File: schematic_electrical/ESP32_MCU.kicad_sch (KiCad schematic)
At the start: 4 parts, among them U1 ESP32_S3_LOLIN

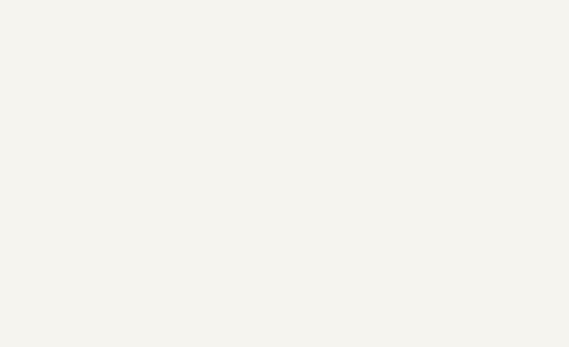
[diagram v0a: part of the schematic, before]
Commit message: Pylon schmatic: clarify filenames and add orange text to avoid confusing other similar schematic pages.
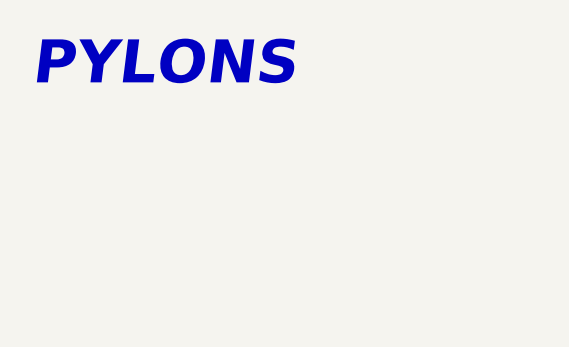
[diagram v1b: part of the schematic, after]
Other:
- note added: "PYLONS"
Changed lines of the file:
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@@
+		)
+	)
+	(text "PYLONS"
+		(exclude_from_sim no)
+		(at 29.972 23.368 0)
+		(effects
+			(font
+				(size 4.7752 4.7752)
+				(thickness 0.955)
+				(bold yes)
+				(italic yes)
+				(color 255 153 0 1)
+			)
 		)
 	)
@@
 		)
 		(instances
-			(project "high_striker_boosh"
+			(project "pylons_boosh_remote_reciver"
 				(path "/f3653ac0-a28a-4ee8-bcf5-236139001455/91617d0d-6f07-4f47-baaa-678bb3c8f5f7"
 					(reference "#PWR02")
@@
 		)
 		(instances
-			(project "high_striker_boosh"
+			(project "pylons_boosh_remote_reciver"
 				(path "/f3653ac0-a28a-4ee8-bcf5-236139001455/91617d0d-6f07-4f47-baaa-678bb3c8f5f7"
 					(reference "#PWR01")
@@
 		)
 		(instances
-			(project "high_striker_boosh"
+			(project "pylons_boosh_remote_reciver"
 				(path "/f3653ac0-a28a-4ee8-bcf5-236139001455/91617d0d-6f07-4f47-baaa-678bb3c8f5f7"
 					(reference "U1")
@@
 		)
 		(instances
-			(project "high_striker_boosh"
+			(project "pylons_boosh_remote_reciver"
 				(path "/f3653ac0-a28a-4ee8-bcf5-236139001455/91617d0d-6f07-4f47-baaa-678bb3c8f5f7"
 					(reference "R11")
@@
 		)
 		(instances
-			(project "high_striker_boosh"
+			(project "pylons_boosh_remote_reciver"
 				(path "/f3653ac0-a28a-4ee8-bcf5-236139001455/91617d0d-6f07-4f47-baaa-678bb3c8f5f7"
 					(reference "#PWR07")
@@
 		)
 		(instances
-			(project "high_striker_boosh"
+			(project "pylons_boosh_remote_reciver"
 				(path "/f3653ac0-a28a-4ee8-bcf5-236139001455/91617d0d-6f07-4f47-baaa-678bb3c8f5f7"
 					(reference "R12")
@@
 		)
 		(instances
-			(project "high_striker_boosh"
+			(project "pylons_boosh_remote_reciver"
 				(path "/f3653ac0-a28a-4ee8-bcf5-236139001455/91617d0d-6f07-4f47-baaa-678bb3c8f5f7"
 					(reference "#PWR04")
@@
 		)
 		(instances
-			(project "high_striker_boosh"
+			(project "pylons_boosh_remote_reciver"
 				(path "/f3653ac0-a28a-4ee8-bcf5-236139001455/91617d0d-6f07-4f47-baaa-678bb3c8f5f7"
 					(reference "R13")
@@
 		)
 		(instances
-			(project "high_striker_boosh"
+			(project "pylons_boosh_remote_reciver"
 				(path "/f3653ac0-a28a-4ee8-bcf5-236139001455/91617d0d-6f07-4f47-baaa-678bb3c8f5f7"
 					(reference "#PWR03")

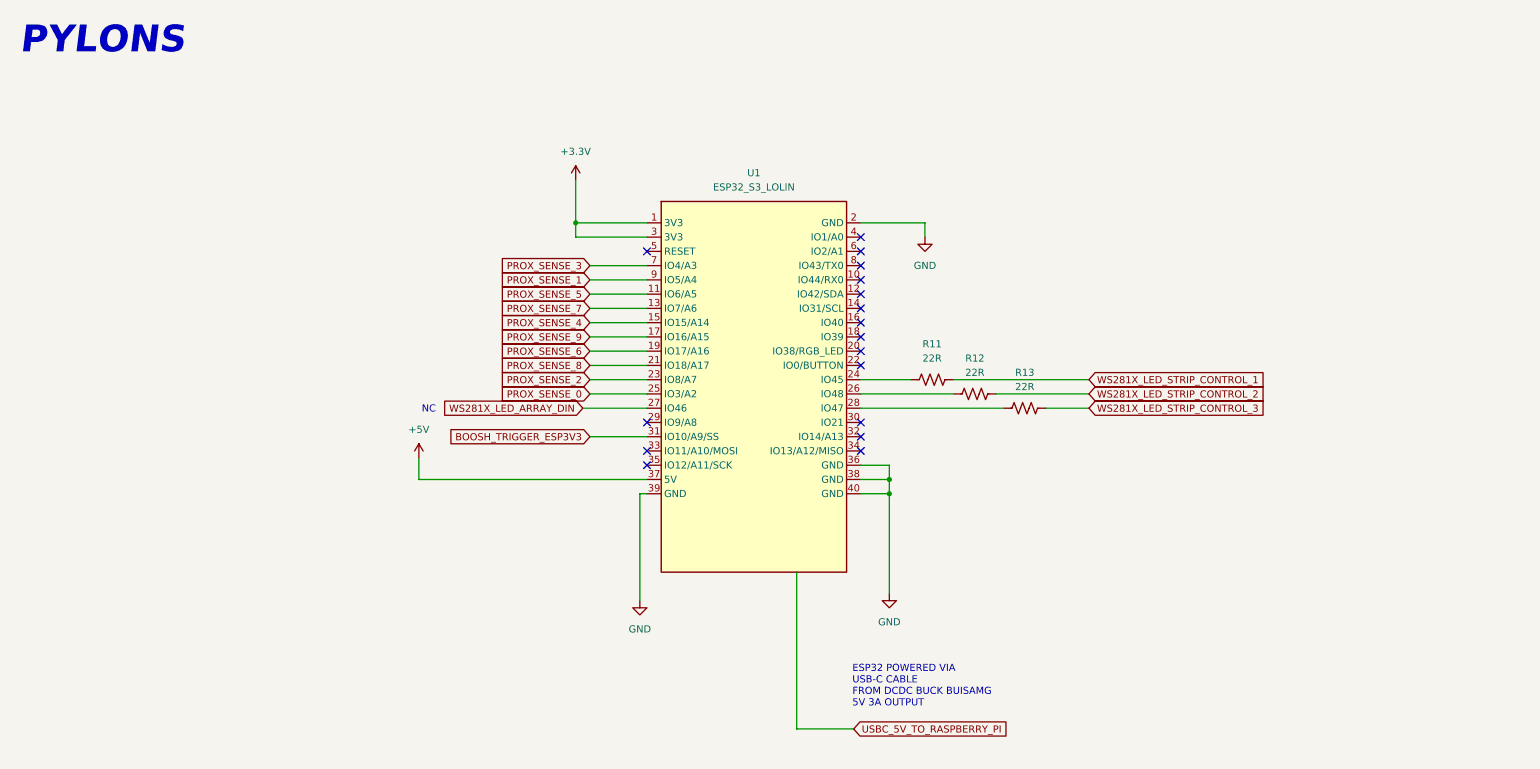
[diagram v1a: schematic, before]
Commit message: Schematic for fabrication. New symbols
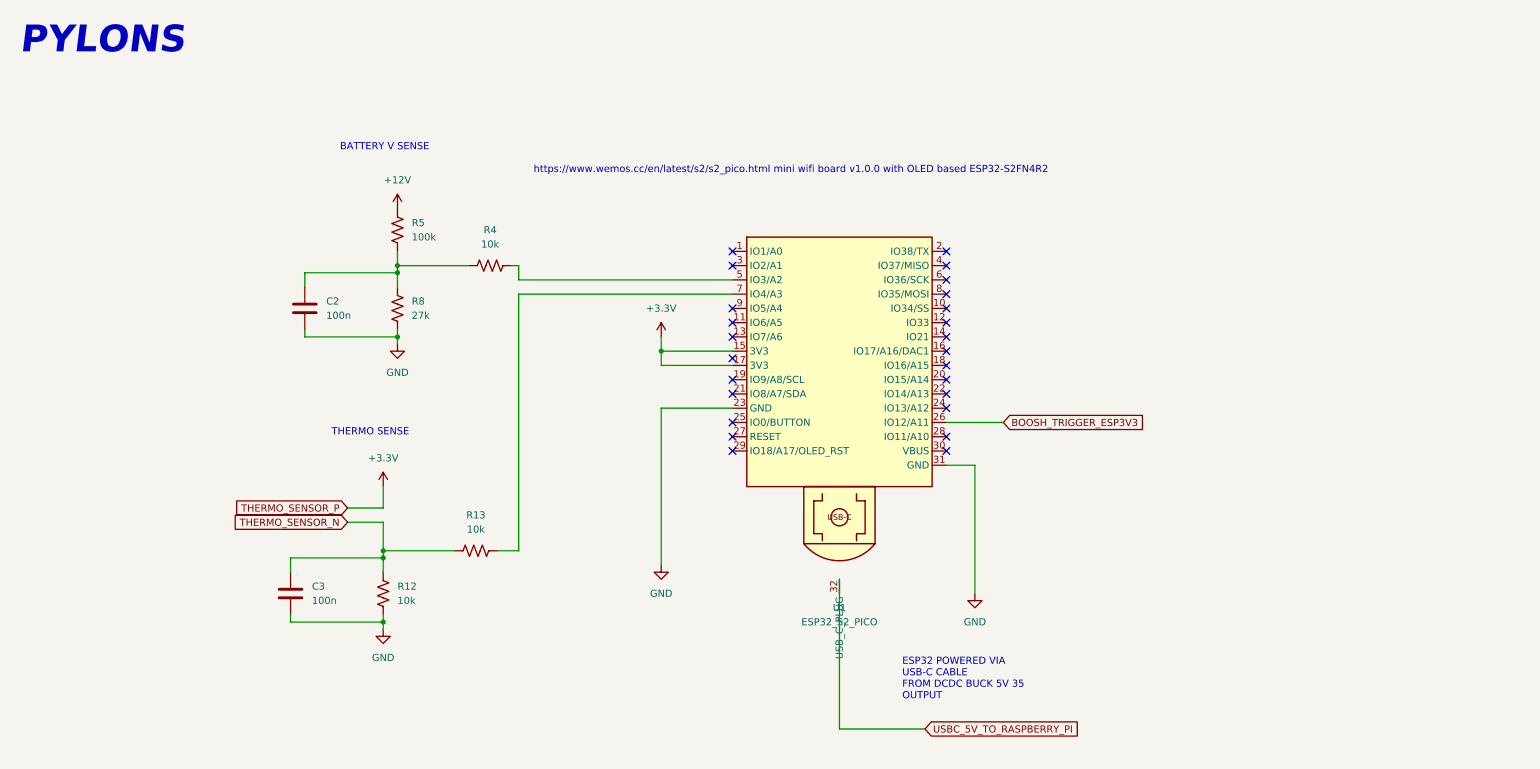
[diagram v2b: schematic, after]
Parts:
- removed R11: 22R, symbol Device:R_US
- removed U1: ESP32_S3_LOLIN, Module:ESP32 S3 LOLIN, symbol esp32 s3 lolin:ESP32_S3_LOLIN
- added C2, C3: 100n, symbol Device:C
- added R4: 10k, symbol Device:R_US
- added R5: 100k, symbol Device:R_US
- added R8: 27k, symbol Device:R_US
- added U1: ESP32_S2_PICO, Module:ESP32_S2_PICO, symbol esp32_s2_pico:ESP32_S2_PICO
- R12, R13: value 22R -> 10k
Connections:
- net WS281X_LED_STRIP_CONTROL_2 is gone; now on net GND: R12.2
- net +3.3V: now also U1.15 (3V3), U1.17 (3V3)
- net BOOSH_TRIGGER_ESP3V3: now also U1.26 (IO12/A11)
- net GND: now also C2.2, C3.2, R8.2, U1.23 (GND), U1.31 (GND)
- net USBC_5V_TO_RASPBERRY_PI: now also U1.32 (USB_C_PLUG)
- net THERMO_SENSOR_N: now reaches R12.1
- net THERMO_SENSOR_N: now also R13.1, C3.1
- net WS281X_LED_STRIP_CONTROL_3: no longer names the net of R13.2
- net WS281X_LED_STRIP_CONTROL_3: now also U1.7 (IO4/A3)
- new net: C2.1, R4.1, R5.2, R8.1
- new net: R4.2, U1.5 (IO3/A2)
- new net +12V: R5.1
- no-connect marks 17 -> 25
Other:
- note added: "BATTERY V SENSE"
- note added: "THERMO SENSE"
- note added: "https://www.wemos.cc/en/latest/s2/s2_pico.html mini wifi board v1.0.0 with OLED based ESP32-S2FN4R2"
- note removed: "NC"

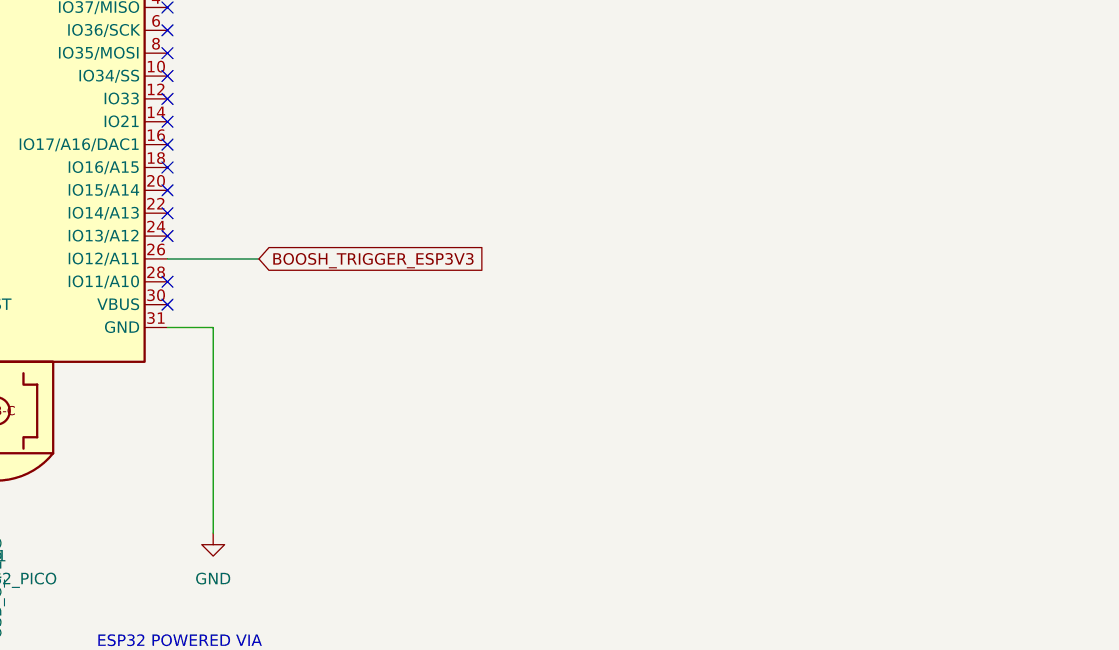
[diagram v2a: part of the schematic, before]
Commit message: scehmatic power options cleanup and LED actual as built
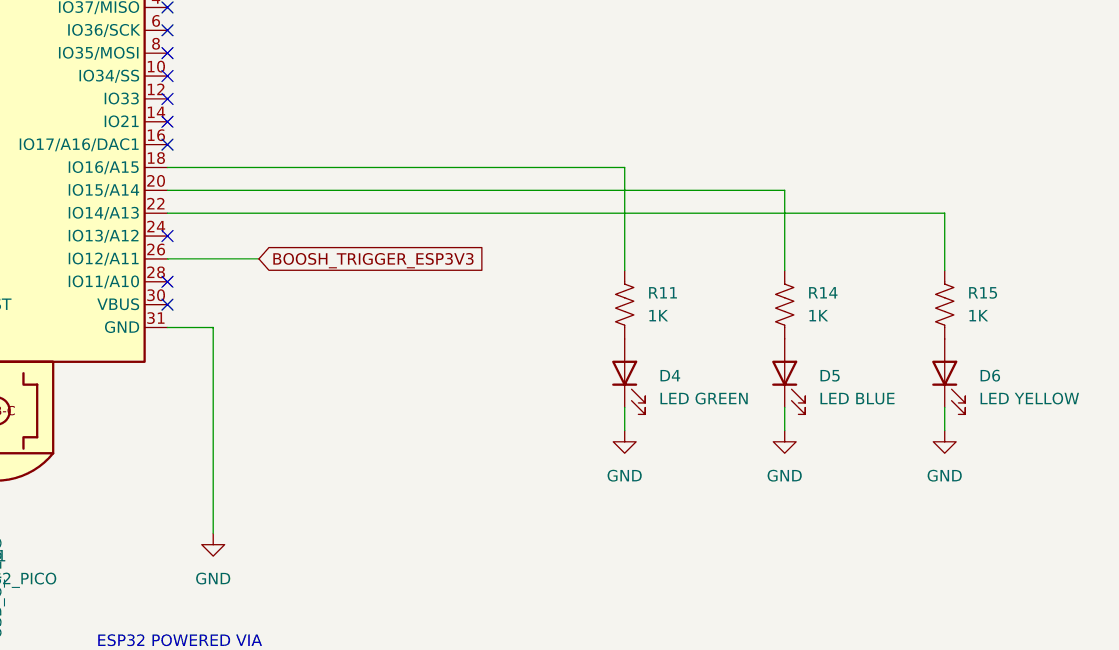
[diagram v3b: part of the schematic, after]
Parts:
- added D4: LED GREEN, symbol Device:LED
- added D5: LED BLUE, symbol Device:LED
- added D6: LED YELLOW, symbol Device:LED
- added R11, R14, R15: 1K, symbol Device:R_US
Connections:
- net GND: now also D4.1 (K), D5.1 (K), D6.1 (K)
- net at U1.18 (IO16/A15): now also R11.2
- net at U1.20 (IO15/A14): now also R14.2
- net at U1.22 (IO14/A13): now also R15.2
- new net: D5.2 (A), R14.1
- new net: D4.2 (A), R11.1
- new net: D6.2 (A), R15.1
- no-connect marks 25 -> 22

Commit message: Schematic symbols and cleanup for building board
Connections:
- net BOOSH_TRIGGER_ESP3V3: now also U1.28 (IO11/A10); no longer U1.26 (IO12/A11)
- net +12V renamed BATTERY_SENSE_12V
- no-connect marks 22 -> 20
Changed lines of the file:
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@@
-	)
-	(no_connect
-		(at 180.34 93.98)
 	)
 	(no_connect
@@
 	)
 	(no_connect
-		(at 180.34 88.9)
-	)
-	(no_connect
 		(at 142.24 93.98)
 	)
@@
 	(wire
 		(pts
+			(xy 72.39 49.53) (xy 82.55 49.53)
+		)
+		(stroke
+			(width 0)
+			(type default)
+		)
+	)
+	(wire
+		(pts
 			(xy 248.92 107.95) (xy 248.92 110.49)
 		)
@@
 	(wire
 		(pts
+			(xy 180.34 93.98) (xy 193.04 93.98)
+		)
+		(stroke
+			(width 0)
+			(type default)
+		)
+	)
+	(wire
+		(pts
 			(xy 142.24 68.58) (xy 104.14 68.58)
 		)
@@
 	(wire
 		(pts
-			(xy 190.5 91.44) (xy 180.34 91.44)
-		)
-		(stroke
-			(width 0)
-			(type default)
-		)
-	)
-	(wire
-		(pts
 			(xy 80.01 128.27) (xy 80.01 127)
 		)
@@
 		(pts
 			(xy 161.29 146.05) (xy 176.53 146.05)
+		)
+		(stroke
+			(width 0)
+			(type default)
+		)
+	)
+	(wire
+		(pts
+			(xy 82.55 49.53) (xy 82.55 53.34)
 		)
 		(stroke
@@
 		)
 	)
+	(global_label "BATTERY_SENSE_12V"
+		(shape input)
+		(at 72.39 49.53 180)
+		(fields_autoplaced yes)
+		(effects
+			(font
+				(size 1.27 1.27)
+			)
+			(justify right)
+		)
+		(property "Intersheetrefs" "${INTERSHEET_REFS}"
+			(at 50.1131 49.53 0)
+			(effects
+				(font
+					(size 1.27 1.27)
+				)
+				(justify right)
+				(hide yes)
+			)
+		)
+	)
 	(global_label "THERMO_SENSOR_P"
 		(shape input)
@@
 	(global_label "BOOSH_TRIGGER_ESP3V3"
 		(shape input)
-		(at 190.5 91.44 0)
+		(at 193.04 93.98 0)
 		(fields_autoplaced yes)
 		(effects
@@
 		)
 		(property "Intersheetrefs" "${INTERSHEET_REFS}"
-			(at 216.8289 91.44 0)
+			(at 219.3689 93.98 0)
 			(effects
 				(font
@@
 					(unit 1)
 				)
-			)
-		)
-	)
-	(symbol
-		(lib_id "power:+12V")
-		(at 82.55 53.34 0)
-		(unit 1)
-		(exclude_from_sim no)
-		(in_bom yes)
-		(on_board yes)
-		(dnp no)
-		(fields_autoplaced yes)
-		(property "Reference" "#PWR08"
-			(at 82.55 57.15 0)
-			(effects
-				(font
-					(size 1.27 1.27)
-				)
-				(hide yes)
-			)
-		)
-		(property "Value" "+12V"
-			(at 82.55 48.26 0)
-			(effects
-				(font
-					(size 1.27 1.27)
-				)
-			)
-		)
-		(property "Footprint" ""
-			(at 82.55 53.34 0)
-			(effects
-				(font
-					(size 1.27 1.27)
-				)
-				(hide yes)
-			)
-		)
-		(property "Datasheet" ""
-			(at 82.55 53.34 0)
-			(effects
-				(font
-					(size 1.27 1.27)
-				)
-				(hide yes)
-			)
-		)
-		(property "Description" "Power symbol creates a global label with name \"+12V\""
-			(at 82.55 53.34 0)
-			(effects
-				(font
-					(size 1.27 1.27)
-				)
-				(hide yes)
-			)
-		)
-		(pin "1"
-		)
-		(instances
-			(project "pylons_boosh_remote_reciver"
-				(path "/f3653ac0-a28a-4ee8-bcf5-236139001455/91617d0d-6f07-4f47-baaa-678bb3c8f5f7"
-					(reference "#PWR08")
-					(unit 1)
-				)

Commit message: Schematic details for as built LED series resistors, BOM/NP variations for bar PYLON
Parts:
- R11, R14, R15: value 1K -> 5.6K
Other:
- note added: "NOT POPULATED ON BAR PYLON AS NO LOCAL TANK FOR THERMO AND USING LINE POWER NOT BATTERY"
- note added: "ONE BOARD MISTAKENLY USES 3X 1R HERE!"
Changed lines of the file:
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@@
+		)
+	)
+	(rectangle
+		(start 41.91 38.1)
+		(end 119.38 151.13)
+		(stroke
+			(width 0)
+			(type dash)
+		)
+		(fill
+			(type none)
 		)
 	)
@@
 		)
 	)
+	(text "NOT POPULATED ON BAR PYLON\nAS NO LOCAL TANK FOR THERMO\nAND USING LINE POWER NOT BATTERY"
+		(exclude_from_sim no)
+		(at 81.026 146.812 0)
+		(effects
+			(font
+				(size 1.27 1.27)
+			)
+		)
+	)
+	(text "ONE BOARD MISTAKENLY \nUSES 3X 1R HERE!"
+		(exclude_from_sim no)
+		(at 268.986 83.566 0)
+		(effects
+			(font
+				(size 1.27 1.27)
+			)
+		)
+	)
 	(text "https://www.wemos.cc/en/latest/s2/s2_pico.html mini wifi board v1.0.0 with OLED based ESP32-S2FN4R2"
 		(exclude_from_sim no)
-		(at 152.654 46.482 0)
+		(at 192.024 51.308 0)
 		(effects
 			(font
@@
 			)
 		)
-		(property "Value" "1K"
+		(property "Value" "5.6K"
 			(at 251.46 97.7899 0)
 			(effects
@@
 			)
 		)
-		(property "Value" "1K"
+		(property "Value" "5.6K"
 			(at 233.68 97.7899 0)
 			(effects
@@
 			)
 		)
-		(property "Value" "1K"
+		(property "Value" "5.6K"
 			(at 269.24 97.7899 0)
 			(effects
